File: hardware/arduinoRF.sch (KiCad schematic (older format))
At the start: 2 parts

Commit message: Added many components to schematic library and schematic changed.
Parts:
- added J?: USB_2, symbol USB_2
- added R?: RES_0603, symbol RES_0603
- added U?: FT232RL, symbol FT232RL
- added U?: BA033CC0WFP, symbol BA033CC0WFP
- added U?: 2450FB15L0001, symbol 2450FB15L0001
- added U?: Q16.000, symbol Q16.000
- added U?: BAT54S, symbol BAT54S
- added U?: LED_RED, symbol LED_RED
- added U?: LED_GREEN, symbol LED_GREEN
- added U?: ICSP, symbol ICSP
- added U?: I2C, symbol I2C
- added U?: DIODE, symbol DIODE
- added U?: SPI, symbol SPI
- added U?: BUTTON, symbol BUTTON
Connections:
- wire segments 0 -> 4
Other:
- note added: "330 ohms"
- note added: "AREA = ???"
- note added: "I2C interface"
- note added: "Programming\nDifference Zigduino and \nArduino duemilanove"
- note added: "Protect DIO = 30\nDIO + AN = 38 PINS\nPIN protection 30 V / 100 mA"
- note added: "SPI interface"
- moved on the sheet: U?A, U?B
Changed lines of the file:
@@
-EESchema Schematic File Version 2  date Tue 03 Apr 2012 01:45:05 PM EEST
+EESchema Schematic File Version 2  date Tue 10 Apr 2012 04:20:07 PM EEST
 LIBS:power
-LIBS:device
-LIBS:transistors
 LIBS:conn
-LIBS:linear
-LIBS:regul
-LIBS:74xx
-LIBS:cmos4000
-LIBS:adc-dac
-LIBS:memory
-LIBS:xilinx
-LIBS:special
-LIBS:microcontrollers
-LIBS:dsp
-LIBS:microchip
-LIBS:analog_switches
-LIBS:motorola
-LIBS:texas
-LIBS:intel
-LIBS:audio
-LIBS:interface
-LIBS:digital-audio
-LIBS:philips
-LIBS:display
-LIBS:cypress
-LIBS:siliconi
-LIBS:opto
-LIBS:atmel
-LIBS:contrib
-LIBS:valves
 LIBS:project_lib
 LIBS:arduinoRF-cache
@@
 Sheet 1 1
 Title ""
-Date "3 apr 2012"
+Date "10 apr 2012"
 Rev ""
 Comp ""
@@
 $EndDescr
 $Comp
+L BUTTON U?
+U 1 1 4F8432E7
+P 3550 3700
+F 0 "U?" H 3550 3600 60  0000 C CNN
+F 1 "BUTTON" H 3550 3840 60  0000 C CNN
+	1    3550 3700
+	1    0    0    -1
+$EndComp
+Text Notes 7700 800  0    35   ~ 0
+I2C interface
+Text Notes 7100 800  0    35   ~ 0
+SPI interface
+Wire Notes Line
+	7500 1300 7500 800
+Wire Notes Line
+	7500 1300 7100 1300
+Wire Notes Line
+	7100 1300 7100 800
+Wire Notes Line
+	7100 800  7500 800
+Wire Notes Line
+	9200 800  8400 800
+Wire Notes Line
+	9200 800  9200 1300
+Wire Notes Line
+	9200 1300 8400 1300
+Wire Notes Line
+	8400 1300 8400 800
+Wire Wire Line
+	9450 1050 9350 1050
+Wire Wire Line
+	9950 1100 10050 1100
+Wire Notes Line
+	9400 1300 10300 1300
+Wire Notes Line
+	9400 1300 9400 900
+Wire Notes Line
+	9400 900  10300 900
+Wire Notes Line
+	10300 900  10300 1300
+Wire Wire Line
+	10250 1100 10350 1100
+Wire Wire Line
+	9450 1150 9350 1150
+Wire Notes Line
+	8200 800  7700 800
+Wire Notes Line
+	8200 800  8200 1300
+Wire Notes Line
+	8200 1300 7700 1300
+Wire Notes Line
+	7700 1300 7700 800
+$Comp
+L SPI U?
+U 1 1 4F84312F
+P 7250 1050
+F 0 "U?" H 7250 900 60  0000 C CNN
+F 1 "SPI" H 7250 1200 60  0000 C CNN
+	1    7250 1050
+	1    0    0    -1
+$EndComp
+$Comp
+L DIODE U?
+U 1 1 4F842F91
+P 2400 3650
+F 0 "U?" H 2400 3550 60  0000 C CNN
+F 1 "DIODE" H 2400 3750 60  0000 C CNN
+	1    2400 3650
+	0    -1   -1   0
+$EndComp
+$Comp
+L I2C U?
+U 1 1 4F842DF5
+P 7900 1050
+F 0 "U?" H 7900 900 60  0000 C CNN
+F 1 "I2C" H 7900 1200 60  0000 C CNN
+	1    7900 1050
+	1    0    0    -1
+$EndComp
+Text Notes 8400 650  0    35   ~ 0
+Programming\nDifference Zigduino and \nArduino duemilanove
+$Comp
+L ICSP U?
+U 1 1 4F842C8A
+P 8800 1050
+F 0 "U?" H 8750 900 60  0000 C CNN
+F 1 "ICSP" H 8800 1200 60  0000 C CNN
+	1    8800 1050
+	1    0    0    -1
+$EndComp
+$Comp
+L LED_GREEN U?
+U 1 1 4F842AEE
+P 2650 3650
+F 0 "U?" H 2650 3500 60  0000 C CNN
+F 1 "LED_GREEN" H 2300 3500 60  0000 C CNN
+	1    2650 3650
+	0    -1   -1   0
+$EndComp
+$Comp
+L LED_RED U?
+U 1 1 4F842A15
+P 2950 3650
+F 0 "U?" H 2950 3500 60  0000 C CNN
+F 1 "LED_RED" H 2650 3500 60  0000 C CNN
+	1    2950 3650
+	0    -1   -1   0
+$EndComp
+Text Notes 9400 1400 0    35   ~ 0
+AREA = ???
+Text Notes 10000 1250 0    31   ~ 0
+330 ohms
+Text Notes 9400 750  0    35   ~ 0
+Protect DIO = 30\nDIO + AN = 38 PINS\nPIN protection 30 V / 100 mA
+$Comp
+L RES_0603 R?
+U 1 1 4F8426CD
+P 10150 1100
+F 0 "R?" H 10150 1175 60  0000 C CNN
+F 1 "RES_0603" H 10150 1200 60  0001 C CNN
+	1    10150 1100
+	1    0    0    -1
+$EndComp
+$Comp
+L BAT54S U?
+U 1 1 4F842680
+P 9700 1100
+F 0 "U?" H 9700 950 60  0000 C CNN
+F 1 "BAT54S" H 9700 1250 60  0000 C CNN
+	1    9700 1100
+	1    0    0    -1
+$EndComp
+$Comp
+L Q16.000 U?
+U 1 1 4F842088
+P 1900 3150
+F 0 "U?" H 1850 3000 60  0000 C CNN
+F 1 "Q16.000" H 1900 3300 60  0000 C CNN
+	1    1900 3150
+	1    0    0    -1
+$EndComp
+$Comp
+L 2450FB15L0001 U?
+U 1 1 4F841D45
+P 5250 1400
+F 0 "U?" H 5400 1200 60  0000 C CNN
+F 1 "2450FB15L0001" H 5250 1600 60  0000 C CNN
+	1    5250 1400
+	-1   0    0    -1
+$EndComp
+$Comp
+L USB_2 J?
+U 1 1 4F8416D6
+P 1000 4800
+F 0 "J?" H 925 5050 60  0000 C CNN
+F 1 "USB_2" H 1050 4500 60  0001 C CNN
+F 4 "VCC" H 1325 4950 50  0001 C CNN "VCC"
+F 5 "D+" H 1300 4850 50  0001 C CNN "Data+"
+F 6 "D-" H 1300 4750 50  0001 C CNN "Data-"
+F 7 "GND" H 1325 4650 50  0001 C CNN "Ground"
+	1    1000 4800
+	1    0    0    -1
+$EndComp
+$Comp
+L BA033CC0WFP U?
+U 1 1 4F841679
+P 2550 6450
+F 0 "U?" H 2500 6250 60  0000 C CNN
+F 1 "BA033CC0WFP" H 2550 6650 60  0000 C CNN
+	1    2550 6450
+	1    0    0    -1
+$EndComp
+$Comp
+L FT232RL U?
+U 1 1 4F841413
+P 2550 5050
+F 0 "U?" H 2400 4500 60  0000 C CNN
+F 1 "FT232RL" H 2500 5600 60  0000 C CNN
+	1    2550 5050
+	1    0    0    -1
+$EndComp
+$Comp
 L ATMEGA128RFA1 U?
 U 1 1 4F7AD218
-P 2900 2850
+P 2050 2000
 AR Path="/4F7AD20E" Ref="U?"  Part="2"
 AR Path="/4F7AD218" Ref="U?"  Part="1"
-F 0 "U?" H 2550 2100 60  0000 C CNN
-F 1 "ATMEGA128RFA1" H 2800 3600 60  0000 C CNN
-	1    2900 2850
+F 0 "U?" H 1700 1250 60  0000 C CNN
+F 1 "ATMEGA128RFA1" H 1950 2750 60  0000 C CNN
+	1    2050 2000
 	1    0    0    -1
 $EndComp
@@
 L ATMEGA128RFA1 U?
 U 2 1 4F7AD20E
-P 4650 2850
-F 0 "U?" H 4300 2100 60  0000 C CNN
-F 1 "ATMEGA128RFA1" H 4550 3600 60  0000 C CNN
-	2    4650 2850
-	1    0    0    -1
-$EndComp
+P 3800 2000
+F 0 "U?" H 3450 1250 60  0000 C CNN
+F 1 "ATMEGA128RFA1" H 3700 2750 60  0000 C CNN
+	2    3800 2000
+	1    0    0    -1
+$EndComp

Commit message: modified components from schematic library and schematic optimized.
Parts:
- added C? (x5): 100n, symbol CAP_0603
- added C?: 4.7u, symbol CAP_0603_POL
- added C? (x2): 10p, symbol CAP_0603
- added J?: J2PIN, symbol J2PIN
- added R? (x8): RES_0603, symbol RES_0603
- added R? (x2): 1K, symbol RES_0603
- added R?: 100, symbol RES_0603
- added U?: LED_RED, symbol LED_RED
- added U?: RX, symbol LED_GREEN
- added U?: TX, symbol LED_GREEN
- added U? (x5): BAT54S, symbol BAT54S
- added X?: DCPWR_JACK2P5_PCB, symbol DCPWR_JACK2P5_PCB
- added X?: CON16, symbol CON16
- added X?: ANALOG, symbol CON6
- U?: value BUTTON -> RESET
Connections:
- net labels added: 5VDC, A0, A0PIN0, A0PIN1, A0PIN2, A0PIN3, A0PIN4, A0PIN5, A0PIN6, A0PIN7, A1, A2, A3, A4, A5, CBUS0, CBUS1, CBUS2, CBUS3, CBUS4, CTS, D+, D-, D0PIN1, D0PIN2, D0PIN3, D0PIN4, D0PIN5, D0PIN6, D0PIN7, D1PIN10, D1PIN11, D1PIN12, D1PIN13, D1PIN8, D1PIN9, DCD, DSR, DTR, GND, PG0, PG1, PG2, PG3, PG4, PG5, RESET, RI, RTS, RXD, TXD, VCC, XXX?
- wire segments 4 -> 172
- no-connect marks 0 -> 9
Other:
- note added: "External connector\nPower Supply\n3.3 - 35 VDC"
- note added: "FTDI outputs"
- note added: "Imax = 1 A"
- note added: "Input: 3.3 - 35 VDC"
- note added: "Output: 3.3 VDC"
- note added: "PWR indicator 3.3V"
- note added: "Power Supply"
- note added: "RESET BUTTON"
- note added: "USB connection"
- note added: "USB to Serial Converter"
- moved on the sheet: R?, U?, U?A, U?B

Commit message: Added arduino kicad reference project, schematic almost finished, board layout.
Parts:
- added C? (x7): 100n, symbol CAP_0603
- added C?: 22p, symbol CAP_0603
- added C?: 1.5p, symbol CAP_0603
- added J?: J3PIN, symbol J3PIN
- added R? (x26): RES_0603, symbol RES_0603
- added R?: 1K, symbol RES_0603
- added U? (x24): BAT54S, symbol BAT54S
- added U?: LED_RED, symbol LED_RED
- added X?: DIGITAL0, symbol CON8
- added X?: DIGITAL1, symbol CON8
- added X?: POWER, symbol CON6
- added X?: DIGITAL2, symbol CON8
- added X?: RP-SMA, symbol RP-SMA
- R?: value RES_0603 -> 1K
- U?: value LED_RED -> RFTX
- U?: value LED_GREEN -> RFRX
- U?: value DIODE -> 1N5819 SMD GLX MELF
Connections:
- net labels added: A1PIN0, A1PIN1, A1PIN2, AREF, D0, D1, D10, D11, D12, D13, D2, D2PIN0, D2PIN1, D2PIN2, D2PIN3, D2PIN4, D2PIN5, D3, D4, D5, D6, D7, D8, D9, DM, DP, RFOUT, RFRX, RFTX, SCL, SDA, VEXT, VIN
- net labels removed: A0PIN6, A0PIN7, D+, D-, D0PIN1
- wire segments 172 -> 446
- no-connect marks 9 -> 10
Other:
- note added: "50 ohm line"
- note added: "50 ohm line on FR4 material 1mm thick\nW = 1.98 mm @ 2.45\nFR4 / thickness 1 mm / 35u metal thickness\nThe effect of solder mask should be investigated."
- note added: "ATmega128RFa1 Analog and RF"
- note added: "ATmega128RFa1 MCU"
- note added: "D0PIN0\nD0PIN1"
- note added: "MISO\nSCK\nRESET"
- note added: "MOSI"
- note added: "Pin 13 LED"
- note added: "Power header"
- note added: "Programming"
- note added: "Should consider about using U.FL connector !"
- note removed: "Programming\nDifference Zigduino and \nArduino duemilanove"
- moved on the sheet: C?, R?, U?, U?A, U?B

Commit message: Added pcb libraries and 3d models for the PCB. Added to some components in schematic datasheets and footprints.
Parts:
- removed J?: USB_2, symbol USB_2
- removed J?: J2PIN, symbol J2PIN
- added J?: USB_B, USB_B, symbol USB_B
- added J? (x2): TEST_PAD, testpoint_2mm5, symbol TEST_PAD
- J?: footprint (none) -> pin_strip_3
- R?: footprint (none) -> r_0603
- U?: footprint (none) -> TO252-5
- U?: footprint (none) -> melf
- U?: footprint (none) -> PCB_PUSH
- X?: footprint (none) -> YDJ-1136
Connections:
- wire segments 446 -> 408
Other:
- moved on the sheet: J?, R?

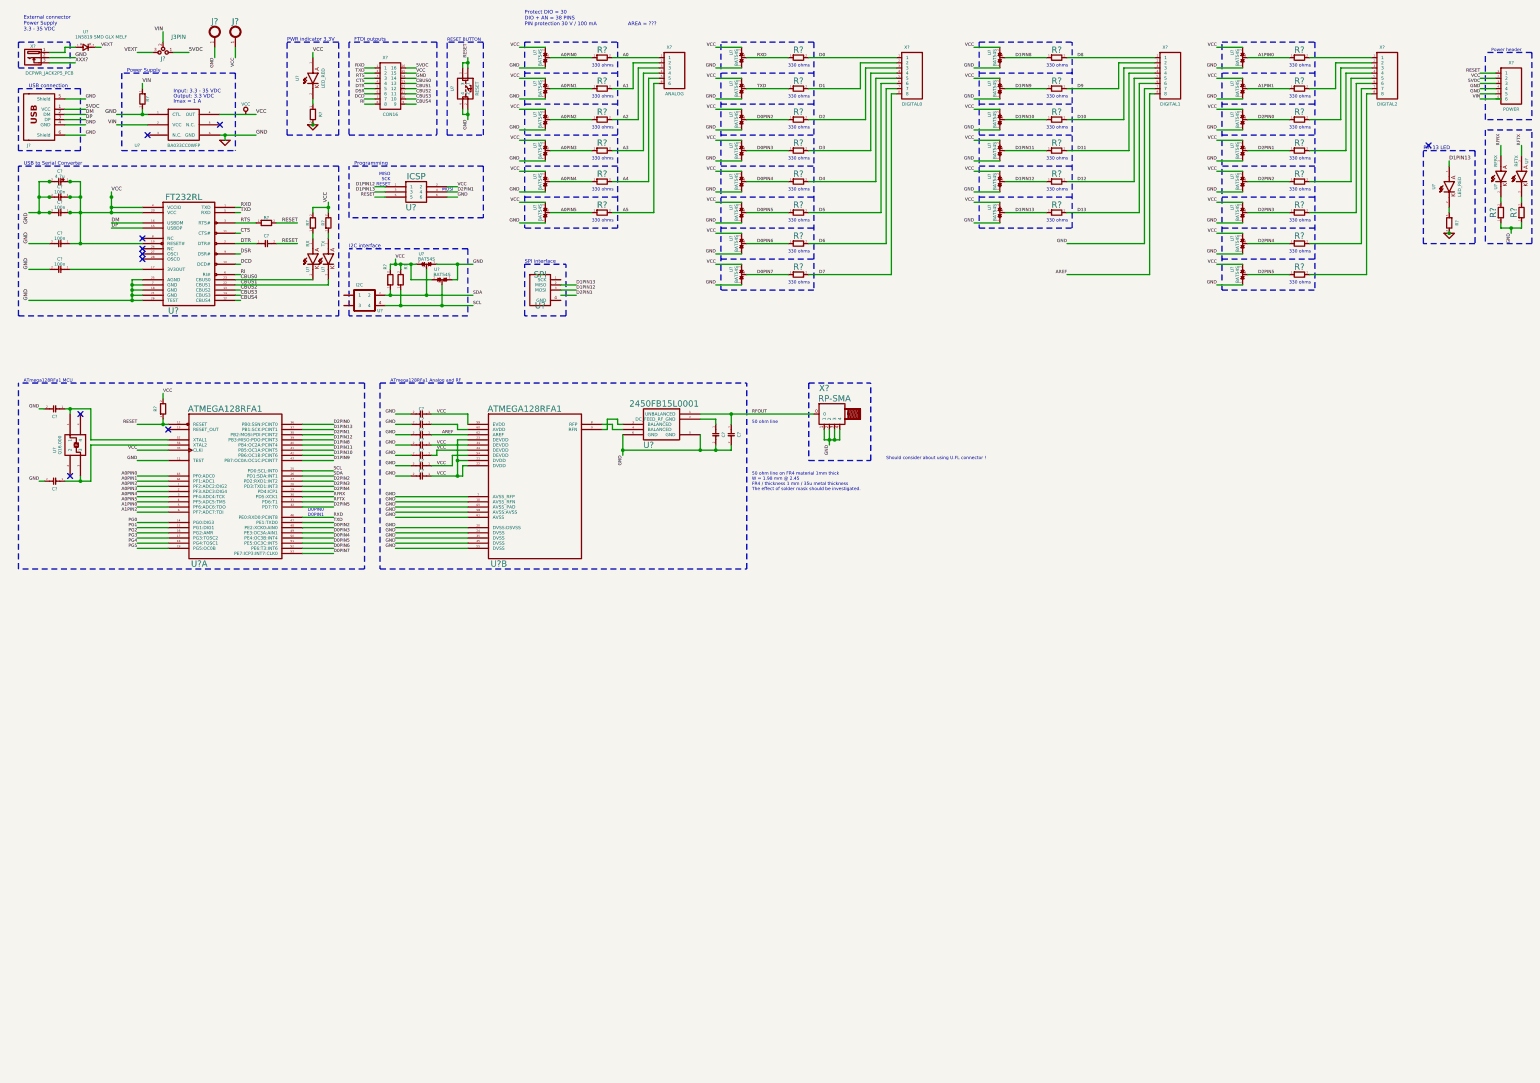
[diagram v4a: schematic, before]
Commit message: Schmatics is more readable now and added most of the modules to the components with references.
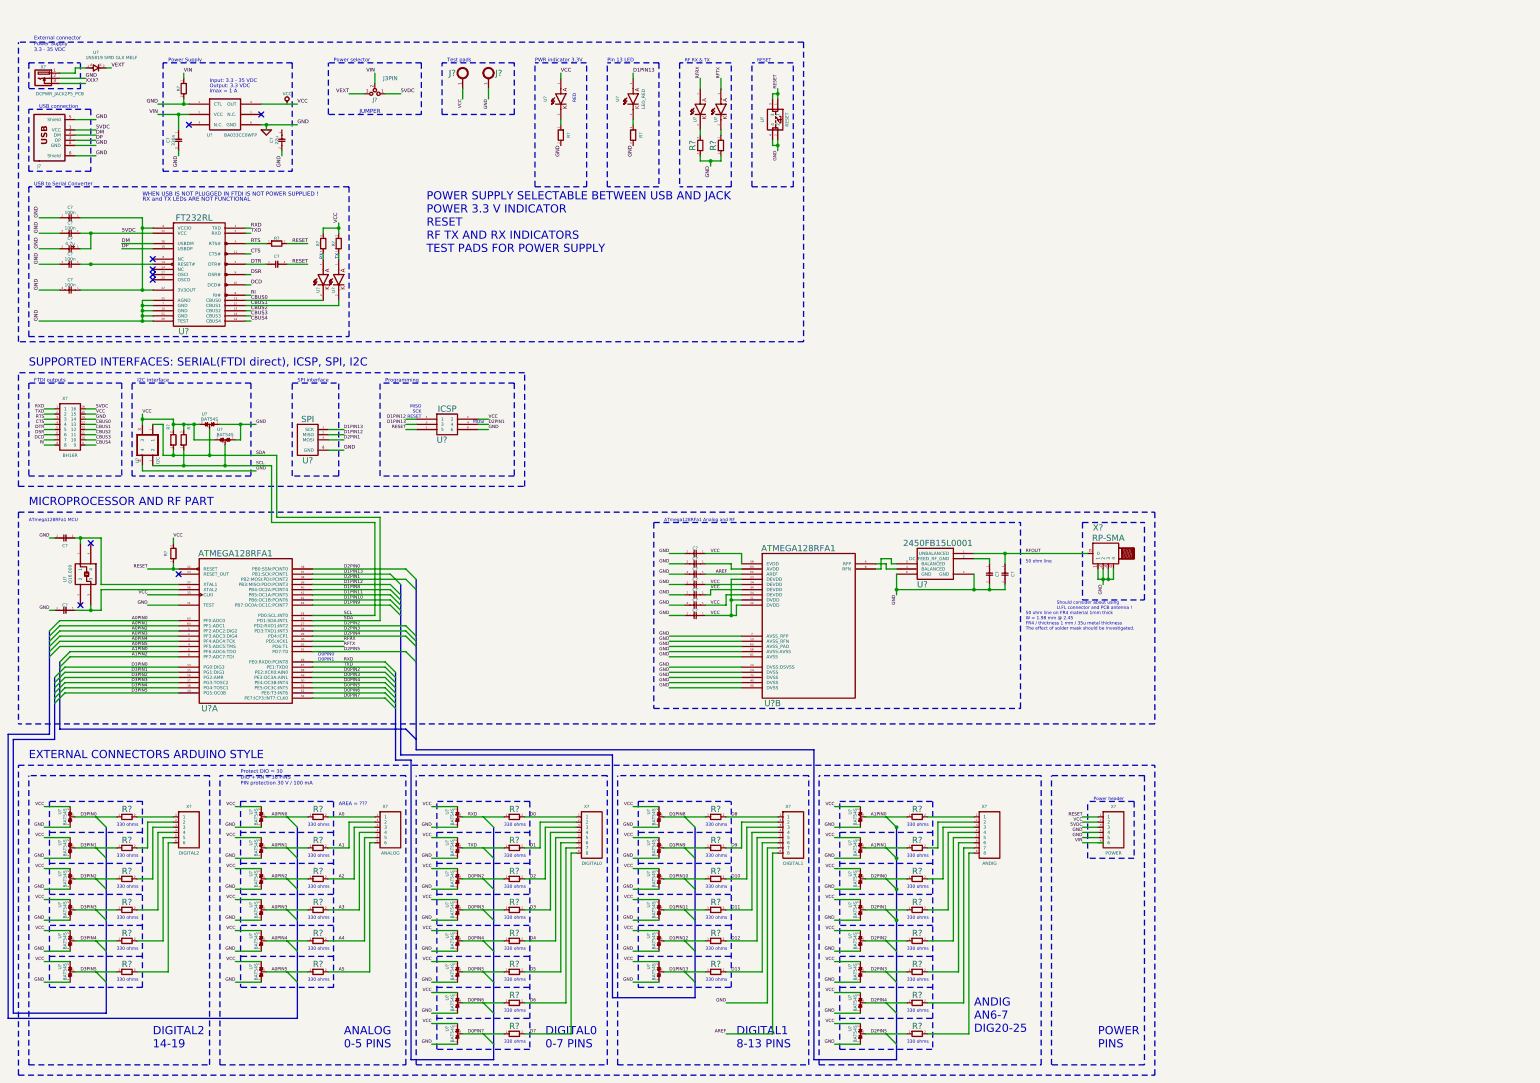
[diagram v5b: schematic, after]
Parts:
- removed R? (x13): RES_0603, symbol RES_0603
- added C?: 330n, c_0603, symbol CAP_0603
- added C?: 22u, c_0805, symbol CAP_0603
- added R? (x13): RES_0603, r_0603, symbol RES_0603
- added R? (x6): RES_0603, symbol RES_0603
- added U? (x6): BAT54S, symbol BAT54S
- added X?: DIGITAL2, symbol CON6
- C? (x16): footprint (none) -> c_0603
- C?: footprint (none) -> c_0805
- R? (x10): footprint (none) -> r_0603
- R?: value RES_0603 -> 10k; footprint (none) -> r_0603
- R? (x2): value RES_0603 -> 1.8K; footprint (none) -> r_0603
- U?: value RFTX -> KP-2012ZGC
- U?: value RFRX -> KP-2012ZGC
- U?: footprint (none) -> pin_strip_3x2
- U?: value LED_RED -> KP-2012SURCK
- U?: value RX -> KP-2012ZGC
- U?: value TX -> KP-2012ZGC
- X?: value CON16 -> BH16R; footprint (none) -> BH16R
- X?: value DIGITAL2 -> ANDIG
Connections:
- net 5VDC: now also C?.1, C?.1, U?.20 (VCC)
- net D0PIN2: now also R?.1
- net D0PIN3: now also R?.1
- net D0PIN4: now also R?.1
- net D0PIN5: now also R?.1
- net D0PIN6: now also R?.1
- net D0PIN7: now also R?.1
- net D1: now also R?.2
- net D10: now also R?.2
- net D11: now also R?.2
- net D12: now also R?.2
- net D13: now also R?.2
- net D1PIN10: now also R?.1
- net D1PIN11: now also R?.1
- net D1PIN12: now also U?.2 (MISO), R?.1; no longer U?.3 (MOSI)
- net D1PIN13: now also U?.1 (SCK), R?.1; no longer U?.2 (MISO)
- net D1PIN8: now also R?.1
- net D1PIN9: now also R?.1
- net D2: now also R?.2
- net D2PIN1: now also U?.3 (MOSI)
- net D3: now also R?.2
- net D4: now also R?.2
- net D5: now also R?.2
- net D6: now also R?.2
- net D7: now also R?.2
- net D8: now also R?.2
- net D9: now also R?.2
- net GND: now also U?.4, U?.4 (GND), C?.2, C?.2, U?.1, U?.1, U?.1, U?.1, U?.1, U?.1
- net SCL: now also U?.2; no longer U?.4
- net SDA: now also U?.1; no longer U?.2
- net TXD: now also R?.1
- net VCC: now also U?.3, U?.2, U?.2, U?.2, U?.2, U?.2, U?.2; no longer C?.1, C?.1, C?.1, C?.1, U?.19 (RESET#), U?.20 (VCC), U?.4 (VCCIO)
- net VIN: now also C?.1
- net at C?.1, U?.17 (3V3OUT): now also C?.1, U?.4 (VCCIO)
- net PG0 renamed D3PIN0
- net D3PIN0: now also R?.1, U?.3
- net PG1 renamed D3PIN1
- net D3PIN1: now also R?.1, U?.3
- net PG2 renamed D3PIN2
- net D3PIN2: now also R?.1, U?.3
- net PG3 renamed D3PIN3
- net D3PIN3: now also R?.1, U?.3
- net PG4 renamed D3PIN4
- net D3PIN4: now also R?.1, U?.3
- net PG5 renamed D3PIN5
- net D3PIN5: now also R?.1, U?.3
- new net: C?.1, U?.19 (RESET#)
- new net: R?.2, X?.5
- new net: R?.2, X?.6
- new net: R?.2, X?.4
- new net: R?.2, X?.3
- new net: R?.2, X?.2
- new net: R?.2, X?.1
- no-connect marks 10 -> 9
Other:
- note added: "ANALOG\n0-5 PINS"
- note added: "ANDIG\nAN6-7\nDIG20-25"
- note added: "DIGITAL0\n0-7 PINS"
- note added: "DIGITAL1\n8-13 PINS"
- note added: "DIGITAL2\n14-19"
- note added: "EXTERNAL CONNECTORS ARDUINO STYLE"
- note added: "JUMPER"
- note added: "MICROPROCESSOR AND RF PART"
- note added: "POWER SUPPLY SELECTABLE BETWEEN USB AND JACK\nPOWER 3.3 V INDICATOR\nRESET\nRF TX AND RX INDICATORS\nTEST PADS FOR POWER SUPPLY\n"
- note added: "POWER\nPINS"
- note added: "Power selector"
- note added: "RED"
- note added: "RESET"
- note added: "RF RX & TX"
- note added: "RX"
- note added: "RX and TX LEDs ARE NOT FUNCTIONAL"
- note added: "SUPPORTED INTERFACES: SERIAL(FTDI direct), ICSP, SPI, I2C"
- note added: "Should consider about using \nU.FL connector and PCB antenna !"
- note added: "TX"
- note added: "Test pads"
- note added: "WHEN USB IS NOT PLUGGED IN FTDI IS NOT POWER SUPPLIED !\n"
- note removed: "RESET BUTTON"
- note removed: "Should consider about using U.FL connector !"
- moved on the sheet: C?, J?, R?, U?, U?A, U?B, X?
